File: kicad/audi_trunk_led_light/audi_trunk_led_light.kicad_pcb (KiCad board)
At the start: 2 copper layers, 96.1 x 42.2 mm, 77 parts, among them P1 CONN_01X02, P2 CONN_01X02

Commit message: clean up
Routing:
- net Net-(P1-Pad1): track 297.5 -> 44.4 mm
- net Net-(D16-PadBC): track 215.2 -> 123.1 mm, vias 7 -> 5
- net Net-(D20-PadBC): track 9.41 -> 16.5 mm
- net Net-(D12-PadGA): track 18.7 -> 24.7 mm
- net Net-(D20-PadRC): track 10.5 -> 13.2 mm
- net Net-(D10-PadGA): track 15.5 -> 12.9 mm
- net Net-(D20-PadGA): track 17.2 -> 18.5 mm
- net Net-(D20-PadGC): track 9.99 -> 11.3 mm
- net Net-(D12-PadRA): track 8.23 -> 9.48 mm
- net Net-(D29-PadGA): track 15.8 -> 16.9 mm
- net Net-(D19-PadBC): track 19.7 -> 20.4 mm
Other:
- net class Default: trace_width 0.2032 -> 0.4

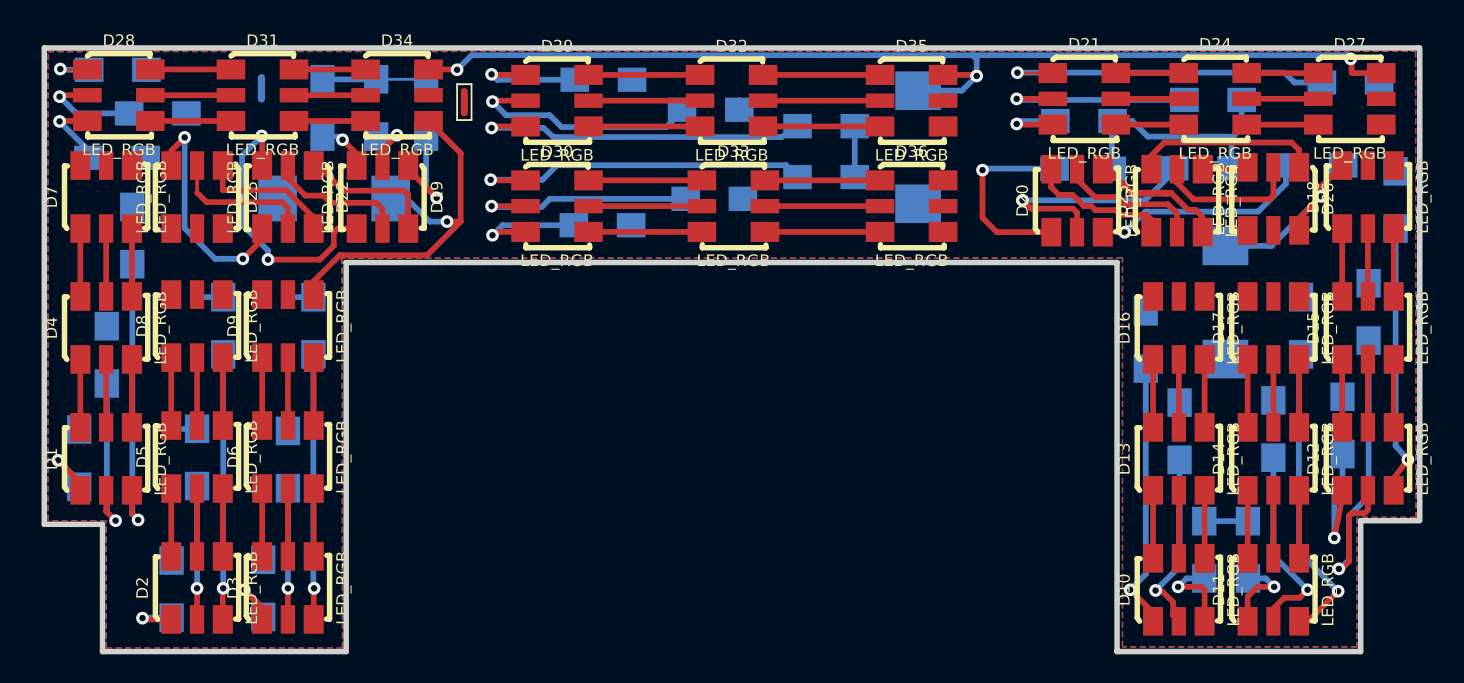
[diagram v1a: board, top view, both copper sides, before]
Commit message: real shape of board
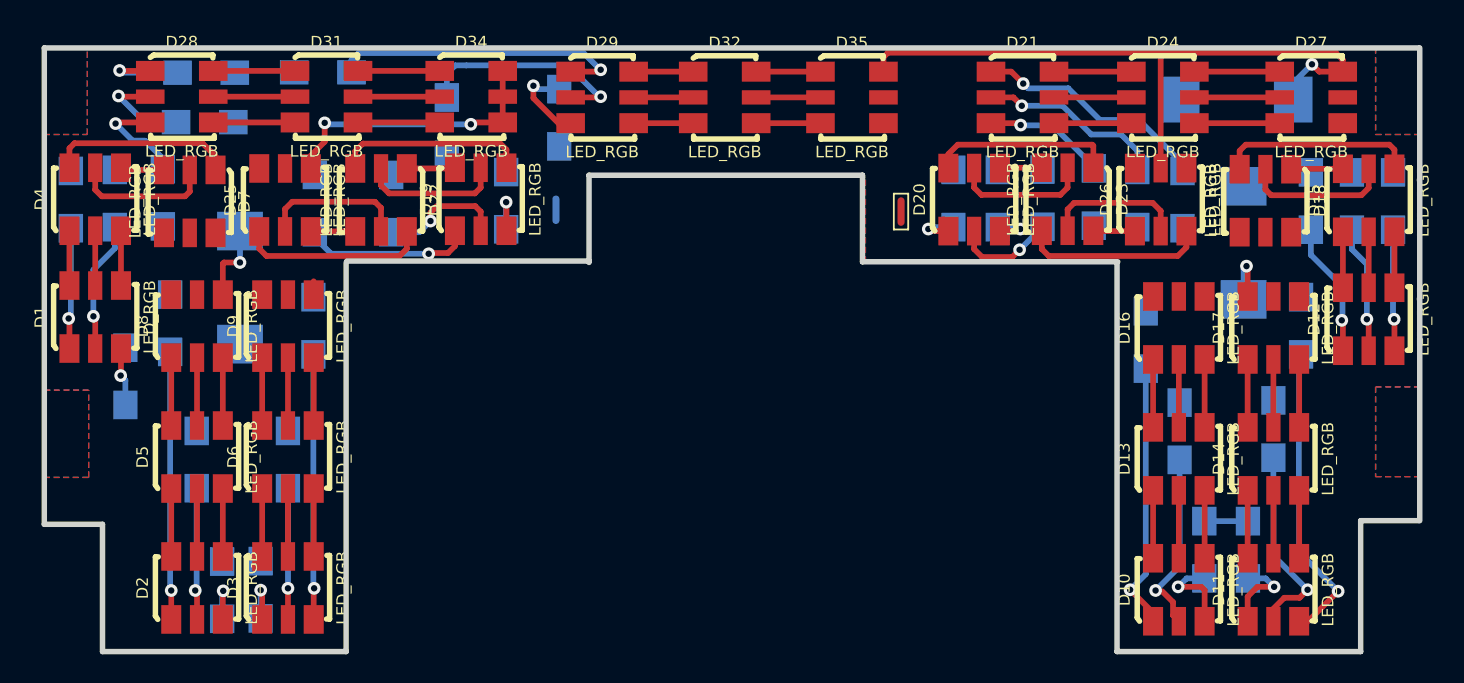
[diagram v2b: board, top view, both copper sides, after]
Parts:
- removed D30, D33, D36: LED_RGB, my_modules:5050_LED
- removed R37, R38, R39: 240, Resistors_SMD:R_1206_HandSoldering
- moved P2 31.4 mm to (186.8, 79.2)
- moved R11 22.5 mm to (210.3, 71.4), turned to 180 degrees
- moved P1 22.3 mm to (162.7, 79.1)
- moved R27 22.2 mm to (193.6, 78.3), turned to 90 degrees
- moved R34 19.6 mm to (146.5, 69.5), turned to 180 degrees
- moved R36 18.7 mm to (163.0, 72.7), turned to 270 degrees
- moved R4 18.6 mm to (135.8, 87.0)
- moved R6 18.5 mm to (139.4, 105.7)
- moved R35 18.5 mm to (155.1, 73.3), turned to 270 degrees
- moved R1 18.1 mm to (128.9, 78.4)
- moved R19 15.8 mm to (215.5, 78.5)
- moved R24 14.4 mm to (159.3, 78.5)
- moved R28 14.3 mm to (206.5, 78.4), turned to 270 degrees
- moved R26 11.4 mm to (196.7, 78.3), turned to 90 degrees
- moved R2 10.9 mm to (131.9, 78.3)
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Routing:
- net Net-(D16-PadBC): track 123.1 -> 81.4 mm
- net Net-(P1-Pad1): track 44.4 -> 5.05 mm
- net Net-(D30-PadRA): track 24.7 -> 0.00 mm, vias 1 -> 0
- net Net-(D29-PadBA): track 24.3 -> 6.09 mm
- net Net-(D30-PadGA): track 16.2 -> 0.00 mm, vias 1 -> 0
- net Net-(D1-PadBA): track 20.3 -> 4.40 mm
- net Net-(D12-PadGA): track 24.7 -> 8.94 mm
- net Net-(D2-PadRA): track 4.09 -> 19.6 mm
- net Net-(D2-PadBA): track 18.5 -> 3.99 mm
- net Net-(D20-PadBC): track 16.5 -> 2.94 mm
- net Net-(D22-PadBC): track 16.3 -> 3.11 mm, vias 2 -> 0
- net Net-(D29-PadRA): track 8.36 -> 21.1 mm
- net Net-(D20-PadGA): track 18.5 -> 7.14 mm
- net Net-(D20-PadBA): track 15.5 -> 4.14 mm
- net Net-(D12-PadBA): track 19.0 -> 8.50 mm
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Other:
- outline, holes or cut-outs redrawn
